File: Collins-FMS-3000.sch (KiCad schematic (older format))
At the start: 23 parts, among them U2 MCP23017_SO, U3 MCP23017_SO, U4 IS31FL3733B

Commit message: Fully routed
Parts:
- removed R1, R2, R3, R4, R8, R9: 2k, Resistor_SMD:R_0805_2012Metric_Pad1.20x1.40mm_HandSolder, symbol Device:R_Small
- removed R5: 100k, Resistor_SMD:R_0402_1005Metric, symbol Device:R_Small
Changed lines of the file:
@@
 	1    0    0    -1
 $EndComp
-Text GLabel 1000 1200 0    50   BiDi ~ 0
+Text GLabel 1400 1200 0    50   BiDi ~ 0
 I2C_SDA
-Text GLabel 1000 1300 0    50   Input ~ 0
+Text GLabel 1400 1300 0    50   Input ~ 0
 I2C_SCL
 NoConn ~ 1400 1800
@@
 $EndComp
 Connection ~ 2100 900
-Text GLabel 5750 1200 2    50   BiDi ~ 0
+Text GLabel 5200 1200 2    50   BiDi ~ 0
 I2C_SDA
-Text GLabel 5750 1300 2    50   Input ~ 0
+Text GLabel 5200 1300 2    50   Input ~ 0
 I2C_SCL
 $Comp
@@
 Wire Wire Line
 	5200 2100 5300 2100
-Connection ~ 4500 900
 NoConn ~ 3800 2500
 NoConn ~ 3800 2600
@@
 Wire Wire Line
 	3300 3250 3100 3250
-$Comp
-L Device:R_Small R1
-U 1 1 618D9439
-P 1100 1050
-F 0 "R1" H 1159 1096 50  0000 L CNN
-F 1 "2k" H 1159 1005 50  0000 L CNN
-F 2 "Resistor_SMD:R_0805_2012Metric_Pad1.20x1.40mm_HandSolder" H 1100 1050 50  0001 C CNN
-F 3 "~" H 1100 1050 50  0001 C CNN
-	1    1100 1050
-	1    0    0    -1
-$EndComp
-$Comp
-L Device:R_Small R2
-U 1 1 618D97E0
-P 1350 1050
-F 0 "R2" H 1409 1096 50  0000 L CNN
-F 1 "2k" H 1409 1005 50  0000 L CNN
-F 2 "Resistor_SMD:R_0805_2012Metric_Pad1.20x1.40mm_HandSolder" H 1350 1050 50  0001 C CNN
-F 3 "~" H 1350 1050 50  0001 C CNN
-	1    1350 1050
-	1    0    0    -1
-$EndComp
-Wire Wire Line
-	1350 1300 1350 1150
-Wire Wire Line
-	1100 1200 1100 1150
-Wire Wire Line
-	1100 1200 1000 1200
-Wire Wire Line
-	1100 950  1100 900
-Wire Wire Line
-	1100 900  1350 900
-Wire Wire Line
-	1350 950  1350 900
-Connection ~ 1350 900
-Wire Wire Line
-	1350 900  2100 900
-Wire Wire Line
-	1400 1300 1350 1300
 Wire Wire Line
 	2100 900  2200 900
-Wire Wire Line
-	1350 1300 1000 1300
-Connection ~ 1350 1300
-Wire Wire Line
-	1100 1200 1400 1200
-Connection ~ 1100 1200
-$Comp
-L Device:R_Small R3
-U 1 1 618ED4A8
-P 5300 1100
-F 0 "R3" H 5359 1146 50  0000 L CNN
-F 1 "2k" H 5359 1055 50  0000 L CNN
-F 2 "Resistor_SMD:R_0805_2012Metric_Pad1.20x1.40mm_HandSolder" H 5300 1100 50  0001 C CNN
-F 3 "~" H 5300 1100 50  0001 C CNN
-	1    5300 1100
-	1    0    0    -1
-$EndComp
-$Comp
-L Device:R_Small R4
-U 1 1 618EDA4E
-P 5550 1100
-F 0 "R4" H 5609 1146 50  0000 L CNN
-F 1 "2k" H 5609 1055 50  0000 L CNN
-F 2 "Resistor_SMD:R_0805_2012Metric_Pad1.20x1.40mm_HandSolder" H 5550 1100 50  0001 C CNN
-F 3 "~" H 5550 1100 50  0001 C CNN
-	1    5550 1100
-	1    0    0    -1
-$EndComp
-Wire Wire Line
-	5200 1300 5300 1300
-Wire Wire Line
-	5300 1300 5300 1200
-Wire Wire Line
-	5300 1000 5300 900
-Connection ~ 5300 900
-Wire Wire Line
-	5300 900  4500 900
-Wire Wire Line
-	5550 900  5550 1000
-Wire Wire Line
-	5300 900  5550 900
-Wire Wire Line
-	5550 1200 5750 1200
-Connection ~ 5550 1200
-Wire Wire Line
-	5300 1300 5750 1300
-Connection ~ 5300 1300
 $Comp
 L power:+5V #PWR0103
@@
 $EndComp
 NoConn ~ 7450 3500
-$Comp
-L Device:R_Small R9
-U 1 1 61A0BFB6
-P 7250 2200
-F 0 "R9" H 7309 2246 50  0000 L CNN
-F 1 "2k" H 7309 2155 50  0000 L CNN
-F 2 "Resistor_SMD:R_0805_2012Metric_Pad1.20x1.40mm_HandSolder" H 7250 2200 50  0001 C CNN
-F 3 "~" H 7250 2200 50  0001 C CNN
-	1    7250 2200
-	1    0    0    -1
-$EndComp
-Wire Wire Line
-	7450 2350 7250 2350
-$Comp
-L Device:R_Small R8
-U 1 1 61A12756
-P 7050 2200
-F 0 "R8" H 7109 2246 50  0000 L CNN
-F 1 "2k" H 7109 2155 50  0000 L CNN
-F 2 "Resistor_SMD:R_0805_2012Metric_Pad1.20x1.40mm_HandSolder" H 7050 2200 50  0001 C CNN
-F 3 "~" H 7050 2200 50  0001 C CNN
-	1    7050 2200
-	1    0    0    -1
-$EndComp
-Wire Wire Line
-	7250 2300 7250 2350
-Wire Wire Line
-	7250 2100 7050 2100
-$Comp
-L power:+5V #PWR012
-U 1 1 61A250CA
-P 7050 2100
-F 0 "#PWR012" H 7050 1950 50  0001 C CNN
-F 1 "+5V" H 7150 2150 50  0000 C CNN
-F 2 "" H 7050 2100 50  0001 C CNN
-F 3 "" H 7050 2100 50  0001 C CNN
-	1    7050 2100
-	1    0    0    -1
-$EndComp
-Connection ~ 7050 2100
-Wire Wire Line
-	7450 2450 7050 2450
-Wire Wire Line
-	7050 2450 7050 2300
-Wire Wire Line
-	7250 2350 6900 2350
-Connection ~ 7250 2350
-Wire Wire Line
-	7050 2450 6900 2450
-Connection ~ 7050 2450
-Text GLabel 6900 2350 0    50   BiDi ~ 0
+Text GLabel 7450 2350 0    50   BiDi ~ 0
 I2C_SDA
-Text GLabel 6900 2450 0    50   BiDi ~ 0
+Text GLabel 7450 2450 0    50   BiDi ~ 0
 I2C_SCL
 NoConn ~ 7450 2650
@@
 $EndComp
 Connection ~ 7950 4200
-Wire Wire Line
-	7450 2550 7050 2550
-Text GLabel 6900 2550 0    50   Input ~ 0
+Text GLabel 7450 2550 0    50   Input ~ 0
 SDB
-$Comp
-L Device:R_Small R5
-U 1 1 61A7BE7A
-P 6550 2850
-F 0 "R5" H 6609 2896 50  0000 L CNN
-F 1 "100k" H 6609 2805 50  0000 L CNN
-F 2 "Resistor_SMD:R_0402_1005Metric" H 6550 2850 50  0001 C CNN
-F 3 "~" H 6550 2850 50  0001 C CNN
-	1    6550 2850
-	1    0    0    -1
-$EndComp
-Wire Wire Line
-	7050 2550 7050 2650
-Wire Wire Line
-	7050 2650 6550 2650
-Wire Wire Line
-	6550 2650 6550 2750
-Connection ~ 7050 2550
-Wire Wire Line
-	7050 2550 6900 2550
-$Comp
-L power:GND #PWR06
-U 1 1 61A8402C
-P 6550 2950
-F 0 "#PWR06" H 6550 2700 50  0001 C CNN
-F 1 "GND" H 6555 2777 50  0000 C CNN
-F 2 "" H 6550 2950 50  0001 C CNN
-F 3 "" H 6550 2950 50  0001 C CNN
-	1    6550 2950
-	1    0    0    -1
-$EndComp
 $Comp
 L Device:R_Small R6
@@
 Wire Notes Line
 	550  650  550  3500
-Wire Wire Line
-	5200 1200 5550 1200
 $EndSCHEMATC

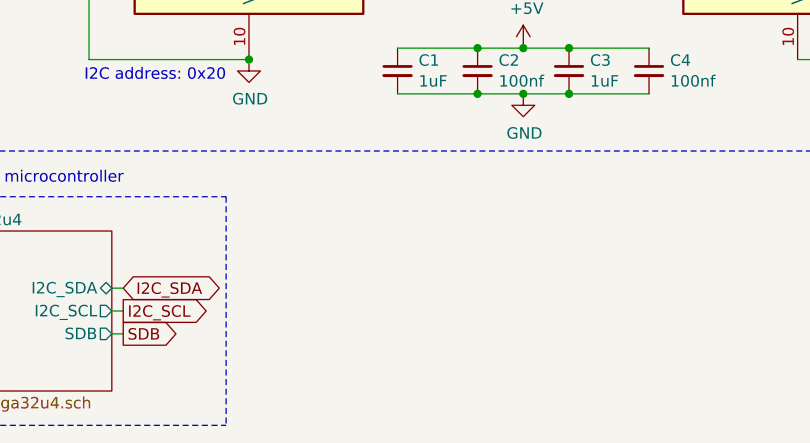
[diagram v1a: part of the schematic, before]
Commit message: Add mounting holes and silkscreen
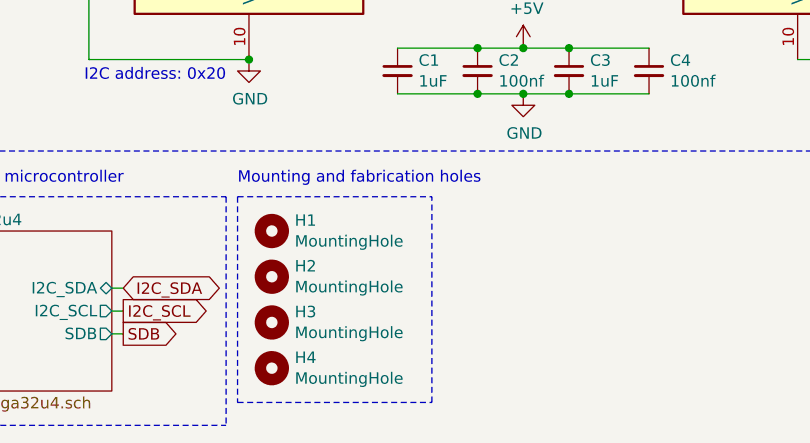
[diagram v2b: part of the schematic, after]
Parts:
- added H1, H2, H3, H4: MountingHole, MountingHole:MountingHole_3.2mm_M3, symbol Mechanical:MountingHole
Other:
- note added: "Mounting and fabrication holes"
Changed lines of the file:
@@
 Wire Notes Line
 	550  650  550  3500
+$Comp
+L Mechanical:MountingHole H1
+U 1 1 618CD3BC
+P 2200 3850
+F 0 "H1" H 2300 3896 50  0000 L CNN
+F 1 "MountingHole" H 2300 3805 50  0000 L CNN
+F 2 "MountingHole:MountingHole_3.2mm_M3" H 2200 3850 50  0001 C CNN
+F 3 "~" H 2200 3850 50  0001 C CNN
+	1    2200 3850
+	1    0    0    -1
+$EndComp
+$Comp
+L Mechanical:MountingHole H2
+U 1 1 618CE0B8
+P 2200 4050
+F 0 "H2" H 2300 4096 50  0000 L CNN
+F 1 "MountingHole" H 2300 4005 50  0000 L CNN
+F 2 "MountingHole:MountingHole_3.2mm_M3" H 2200 4050 50  0001 C CNN
+F 3 "~" H 2200 4050 50  0001 C CNN
+	1    2200 4050
+	1    0    0    -1
+$EndComp
+$Comp
+L Mechanical:MountingHole H3
+U 1 1 618D2A7D
+P 2200 4250
+F 0 "H3" H 2300 4296 50  0000 L CNN
+F 1 "MountingHole" H 2300 4205 50  0000 L CNN
+F 2 "MountingHole:MountingHole_3.2mm_M3" H 2200 4250 50  0001 C CNN
+F 3 "~" H 2200 4250 50  0001 C CNN
+	1    2200 4250
+	1    0    0    -1
+$EndComp
+$Comp
+L Mechanical:MountingHole H4
+U 1 1 618D732D
+P 2200 4450
+F 0 "H4" H 2300 4496 50  0000 L CNN
+F 1 "MountingHole" H 2300 4405 50  0000 L CNN
+F 2 "MountingHole:MountingHole_3.2mm_M3" H 2200 4450 50  0001 C CNN
+F 3 "~" H 2200 4450 50  0001 C CNN
+	1    2200 4450
+	1    0    0    -1
+$EndComp
+Wire Notes Line
+	2050 3700 2050 4600
+Wire Notes Line
+	2050 4600 2900 4600
+Wire Notes Line
+	2900 4600 2900 3700
+Wire Notes Line
+	2050 3700 2900 3700
+Text Notes 2050 3650 0    50   ~ 0
+Mounting and fabrication holes
 $EndSCHEMATC

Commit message: Assign JLCPCB part numbers
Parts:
- C1, C3: JLC (none) -> 0402; LCSC (none) -> C52923
- C2, C25, C26, C27, C4: JLC (none) -> 0402; LCSC (none) -> C1525
- C22, C23, C24, C28: JLC (none) -> 0402; LCSC (none) -> C47339
- R6: JLC (none) -> 0402; LCSC (none) -> C25765
- R7: JLC (none) -> 0402; LCSC (none) -> C25741
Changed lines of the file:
@@
 F 2 "Capacitor_SMD:C_0402_1005Metric" H 3100 3150 50  0001 C CNN
 F 3 "~" H 3100 3150 50  0001 C CNN
+F 4 "0402" H 3100 3150 50  0001 C CNN "JLC"
+F 5 "C1525" H 3100 3150 50  0001 C CNN "LCSC"
 	1    3100 3150
 	1    0    0    -1
@@
 F 2 "Capacitor_SMD:C_0402_1005Metric" H 2750 3150 50  0001 C CNN
 F 3 "~" H 2750 3150 50  0001 C CNN
+F 4 "0402" H 2750 3150 50  0001 C CNN "JLC"
+F 5 "C52923" H 2750 3150 50  0001 C CNN "LCSC"
 	1    2750 3150
 	1    0    0    -1
@@
 F 2 "Capacitor_SMD:C_0402_1005Metric" H 3850 3150 50  0001 C CNN
 F 3 "~" H 3850 3150 50  0001 C CNN
+F 4 "0402" H 3850 3150 50  0001 C CNN "JLC"
+F 5 "C1525" H 3850 3150 50  0001 C CNN "LCSC"
 	1    3850 3150
 	1    0    0    -1
@@
 F 2 "Capacitor_SMD:C_0402_1005Metric" H 3500 3150 50  0001 C CNN
 F 3 "~" H 3500 3150 50  0001 C CNN
+F 4 "0402" H 3500 3150 50  0001 C CNN "JLC"
+F 5 "C52923" H 3500 3150 50  0001 C CNN "LCSC"
 	1    3500 3150
 	1    0    0    -1
@@
 F 2 "Capacitor_SMD:C_0402_1005Metric" H 6800 1200 50  0001 C CNN
 F 3 "~" H 6800 1200 50  0001 C CNN
+F 4 "0402" H 6800 1200 50  0001 C CNN "JLC"
+F 5 "C47339" H 6800 1200 50  0001 C CNN "LCSC"
 	1    6800 1200
 	1    0    0    -1
@@
 F 2 "Capacitor_SMD:C_0402_1005Metric" H 7200 1200 50  0001 C CNN
 F 3 "~" H 7200 1200 50  0001 C CNN
+F 4 "0402" H 7200 1200 50  0001 C CNN "JLC"
+F 5 "C1525" H 7200 1200 50  0001 C CNN "LCSC"
 	1    7200 1200
 	1    0    0    -1
@@
 F 2 "Capacitor_SMD:C_0402_1005Metric" H 6800 1500 50  0001 C CNN
 F 3 "~" H 6800 1500 50  0001 C CNN
+F 4 "0402" H 6800 1500 50  0001 C CNN "JLC"
+F 5 "C47339" H 6800 1500 50  0001 C CNN "LCSC"
 	1    6800 1500
 	1    0    0    -1
@@
 F 2 "Capacitor_SMD:C_0402_1005Metric" H 7200 1500 50  0001 C CNN
 F 3 "~" H 7200 1500 50  0001 C CNN
+F 4 "0402" H 7200 1500 50  0001 C CNN "JLC"
+F 5 "C1525" H 7200 1500 50  0001 C CNN "LCSC"
 	1    7200 1500
 	1    0    0    -1
@@
 F 2 "Capacitor_SMD:C_0402_1005Metric" H 6800 1850 50  0001 C CNN
 F 3 "~" H 6800 1850 50  0001 C CNN
+F 4 "0402" H 6800 1850 50  0001 C CNN "JLC"
+F 5 "C47339" H 6800 1850 50  0001 C CNN "LCSC"
 	1    6800 1850
 	1    0    0    -1
@@
 F 2 "Capacitor_SMD:C_0402_1005Metric" H 7200 1850 50  0001 C CNN
 F 3 "~" H 7200 1850 50  0001 C CNN
+F 4 "0402" H 7200 1850 50  0001 C CNN "JLC"
+F 5 "C1525" H 7200 1850 50  0001 C CNN "LCSC"
 	1    7200 1850
 	1    0    0    -1
@@
 F 2 "Capacitor_SMD:C_0402_1005Metric" H 7200 3150 50  0001 C CNN
 F 3 "~" H 7200 3150 50  0001 C CNN
+F 4 "0402" H 7200 3150 50  0001 C CNN "JLC"
+F 5 "C47339" H 7200 3150 50  0001 C CNN "LCSC"
 	1    7200 3150
 	1    0    0    -1
@@
 F 2 "Resistor_SMD:R_0402_1005Metric" H 6850 2850 50  0001 C CNN
 F 3 "~" H 6850 2850 50  0001 C CNN
+F 4 "0402" H 6850 2850 50  0001 C CNN "JLC"
+F 5 "C25741" H 6850 2850 50  0001 C CNN "LCSC"
 	1    6850 2850
 	1    0    0    -1
@@
 F 2 "Resistor_SMD:R_0402_1005Metric" H 6700 3700 50  0001 C CNN
 F 3 "~" H 6700 3700 50  0001 C CNN
+F 4 "0402" H 6700 3700 50  0001 C CNN "JLC"
+F 5 "C25765" H 6700 3700 50  0001 C CNN "LCSC"
 	1    6700 3700
 	1    0    0    -1

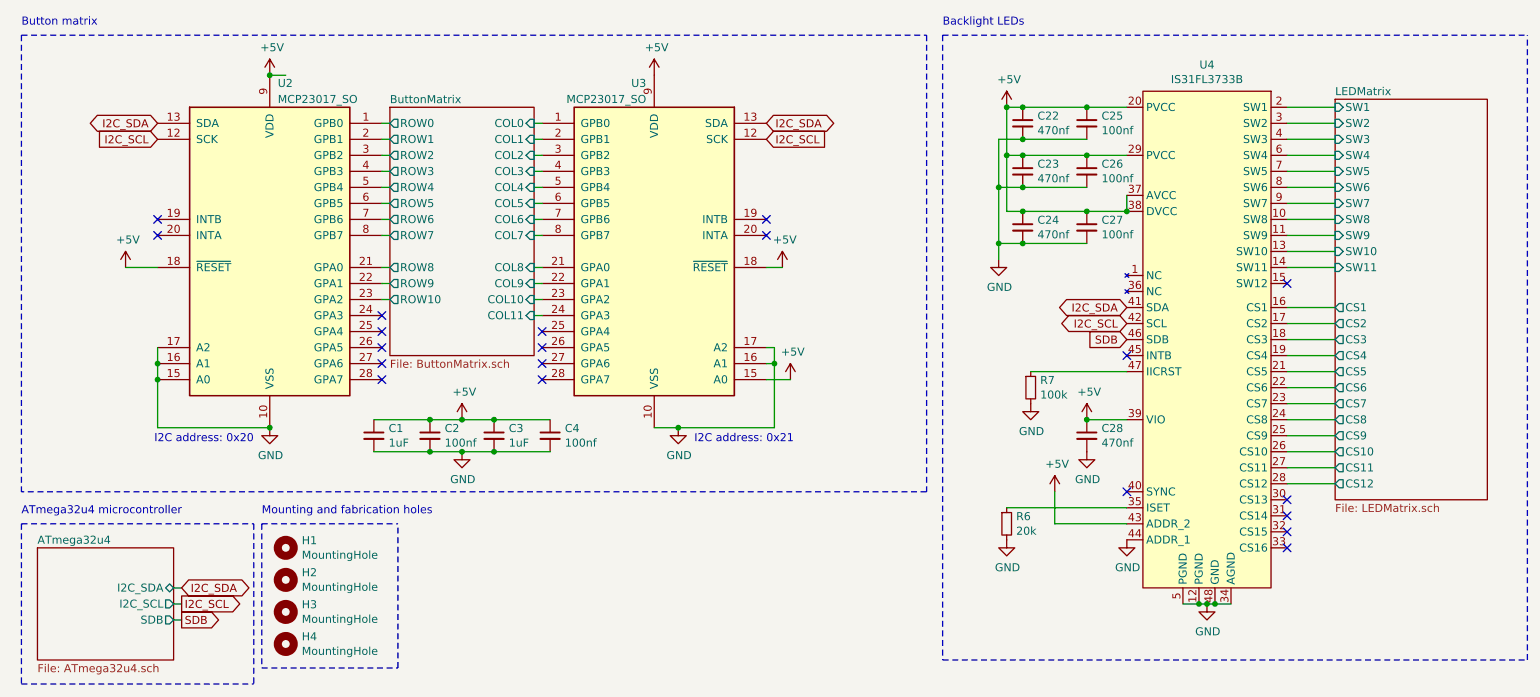
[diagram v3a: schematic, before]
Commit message: Fix the button layout. Still needs trace work.
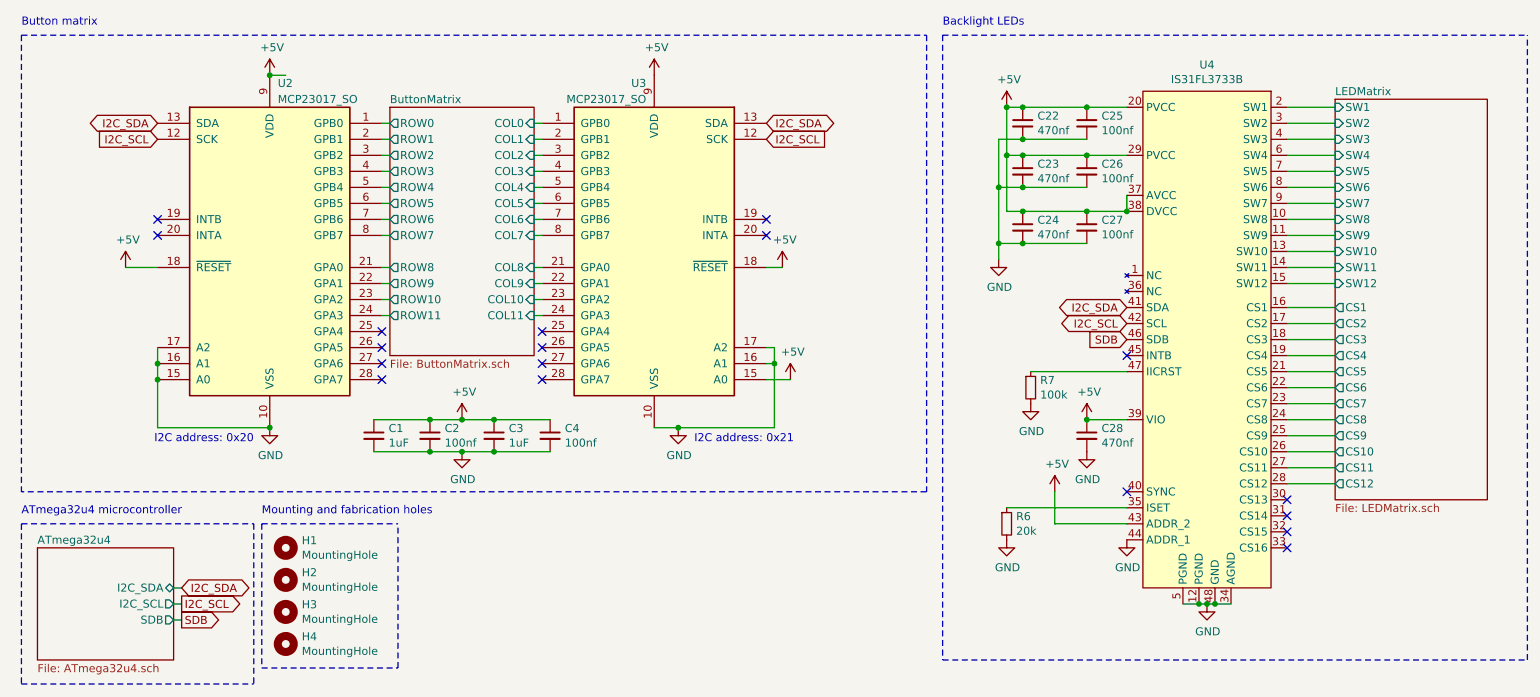
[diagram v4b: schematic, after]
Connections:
- net LEDMatrix/SW12: now reaches U4.15 (SW12)
- net ButtonMatrix/ROW11: now reaches U2.24 (GPA3)
- no-connect marks 20 -> 18
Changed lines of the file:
@@
 F23 "COL10" I R 3750 2300 50
 F24 "COL11" I R 3750 2400 50
+F25 "ROW11" O L 2850 2400 50
 $EndSheet
 $Comp
@@
 NoConn ~ 3800 2700
 NoConn ~ 3800 2800
-NoConn ~ 2800 2400
 NoConn ~ 2800 2500
 NoConn ~ 2800 2600
@@
 F23 "SW11" I L 8750 2100 50
 F24 "CS12" O L 8750 3450 50
+F25 "SW12" I L 8750 2200 50
 $EndSheet
 Wire Wire Line
@@
 Wire Wire Line
 	1500 4200 1550 4200
-NoConn ~ 8450 2200
 NoConn ~ 8450 3550
 NoConn ~ 8450 3650
@@
 Text Notes 2050 3650 0    50   ~ 0
 Mounting and fabrication holes
+Wire Wire Line
+	2800 2400 2850 2400
+Wire Wire Line
+	8750 2200 8450 2200
 $EndSCHEMATC

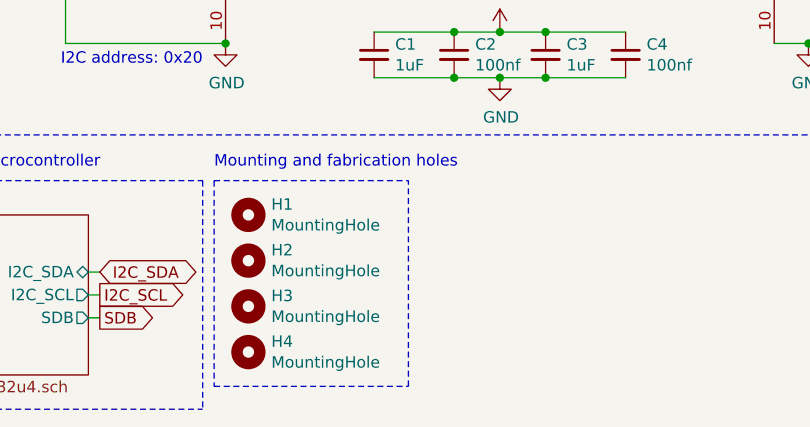
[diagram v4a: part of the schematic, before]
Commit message: Round edges, clean up traces, add placement marks
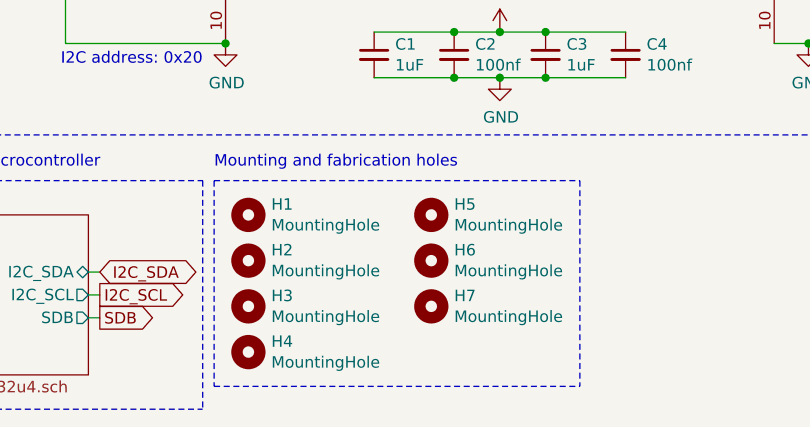
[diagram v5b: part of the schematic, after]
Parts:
- added H5, H6, H7: MountingHole, Collins-FMS-3000:JLCPCB_Tooling_Hole, symbol Mechanical:MountingHole
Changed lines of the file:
@@
 Wire Notes Line
 	2050 3700 2050 4600
-Wire Notes Line
-	2050 4600 2900 4600
-Wire Notes Line
-	2900 4600 2900 3700
-Wire Notes Line
-	2050 3700 2900 3700
 Text Notes 2050 3650 0    50   ~ 0
 Mounting and fabrication holes
@@
 Wire Wire Line
 	8750 2200 8450 2200
+$Comp
+L Mechanical:MountingHole H5
+U 1 1 618DF41E
+P 3000 3850
+F 0 "H5" H 3100 3896 50  0000 L CNN
+F 1 "MountingHole" H 3100 3805 50  0000 L CNN
+F 2 "Collins-FMS-3000:JLCPCB_Tooling_Hole" H 3000 3850 50  0001 C CNN
+F 3 "~" H 3000 3850 50  0001 C CNN
+	1    3000 3850
+	1    0    0    -1
+$EndComp
+$Comp
+L Mechanical:MountingHole H6
+U 1 1 618DF424
+P 3000 4050
+F 0 "H6" H 3100 4096 50  0000 L CNN
+F 1 "MountingHole" H 3100 4005 50  0000 L CNN
+F 2 "Collins-FMS-3000:JLCPCB_Tooling_Hole" H 3000 4050 50  0001 C CNN
+F 3 "~" H 3000 4050 50  0001 C CNN
+	1    3000 4050
+	1    0    0    -1
+$EndComp
+$Comp
+L Mechanical:MountingHole H7
+U 1 1 618DF42A
+P 3000 4250
+F 0 "H7" H 3100 4296 50  0000 L CNN
+F 1 "MountingHole" H 3100 4205 50  0000 L CNN
+F 2 "Collins-FMS-3000:JLCPCB_Tooling_Hole" H 3000 4250 50  0001 C CNN
+F 3 "~" H 3000 4250 50  0001 C CNN
+	1    3000 4250
+	1    0    0    -1
+$EndComp
+Wire Notes Line
+	3650 3700 3650 4600
+Wire Notes Line
+	2050 4600 3650 4600
+Wire Notes Line
+	2050 3700 3650 3700
 $EndSCHEMATC

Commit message: Add INTB connection
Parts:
- added R4: 100k, Resistor_SMD:R_0402_1005Metric, symbol Device:R_Small
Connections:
- net +5V: now also R4.1
- net INTB: now reaches U4.45 (INTB)
- net INTB: now also R4.2
- no-connect marks 18 -> 17
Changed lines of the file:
@@
 F3 "I2C_SCL" O R 1500 4200 50
 F4 "SDB" O R 1500 4300 50
+F5 "INTB" I R 1500 4400 50
 $EndSheet
 Text GLabel 1550 4100 2    50   BiDi ~ 0
@@
 Text GLabel 7450 2450 0    50   BiDi ~ 0
 I2C_SCL
-NoConn ~ 7450 2650
 $Comp
 L Device:R_Small R7
@@
 Wire Notes Line
 	2050 3700 3650 3700
+Text GLabel 6650 2650 0    50   Output ~ 0
+INTB
+Wire Wire Line
+	7450 2650 6850 2650
+$Comp
+L Device:R_Small R4
+U 1 1 61926829
+P 6850 2550
+F 0 "R4" H 6909 2596 50  0000 L CNN
+F 1 "100k" H 6909 2505 50  0000 L CNN
+F 2 "Resistor_SMD:R_0402_1005Metric" H 6850 2550 50  0001 C CNN
+F 3 "~" H 6850 2550 50  0001 C CNN
+	1    6850 2550
+	1    0    0    -1
+$EndComp
+Connection ~ 6850 2650
+Wire Wire Line
+	6850 2650 6650 2650
+$Comp
+L power:+5V #PWR017
+U 1 1 61927283
+P 6850 2450
+F 0 "#PWR017" H 6850 2300 50  0001 C CNN
+F 1 "+5V" H 6865 2623 50  0000 C CNN
+F 2 "" H 6850 2450 50  0001 C CNN
+F 3 "" H 6850 2450 50  0001 C CNN
+	1    6850 2450
+	1    0    0    -1
+$EndComp
+Text GLabel 1550 4400 2    50   Input ~ 0
+INTB
+Wire Wire Line
+	1550 4400 1500 4400
 $EndSCHEMATC
